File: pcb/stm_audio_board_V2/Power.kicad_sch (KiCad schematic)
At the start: 27 parts, among them U2 OP275, U4 OP275, U5 AMS1117-3.3, U8 L78M09CDT, U9 LF33_TO252

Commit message: Update .mxproject, subdir.mk, and 1078 more files...
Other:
- note added: "18V to 5V COMMON TODO"
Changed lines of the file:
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@@
+    (fill (type none))
+  )
+  (rectangle (start 16.51 74.93) (end 120.65 121.92)
+    (stroke (width 0) (type default))
     (fill (type none))
   )
@@
     (effects (font (size 1.27 1.27)) (justify left bottom))
   )
+  (text "18V to 5V COMMON TODO\n" (at 16.51 73.66 0)
+    (effects (font (size 1.27 1.27)) (justify left bottom))
+  )

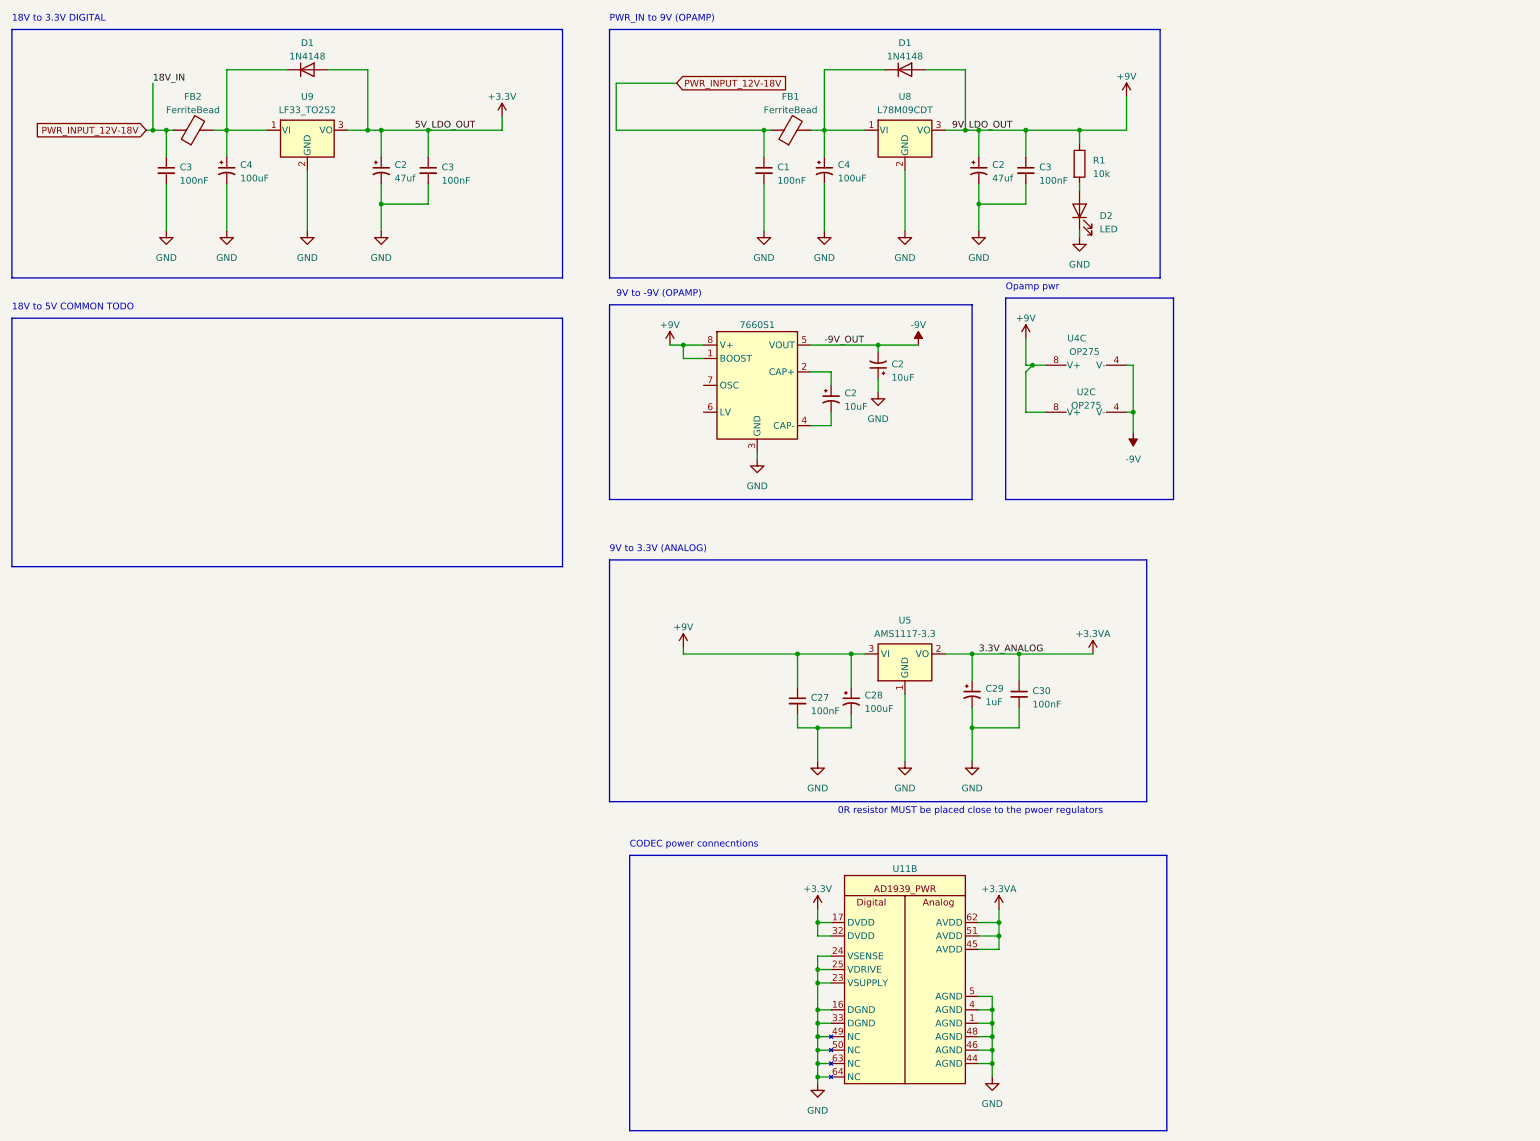
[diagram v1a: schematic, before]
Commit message: pinout added, pcb is updated according to pinout excel
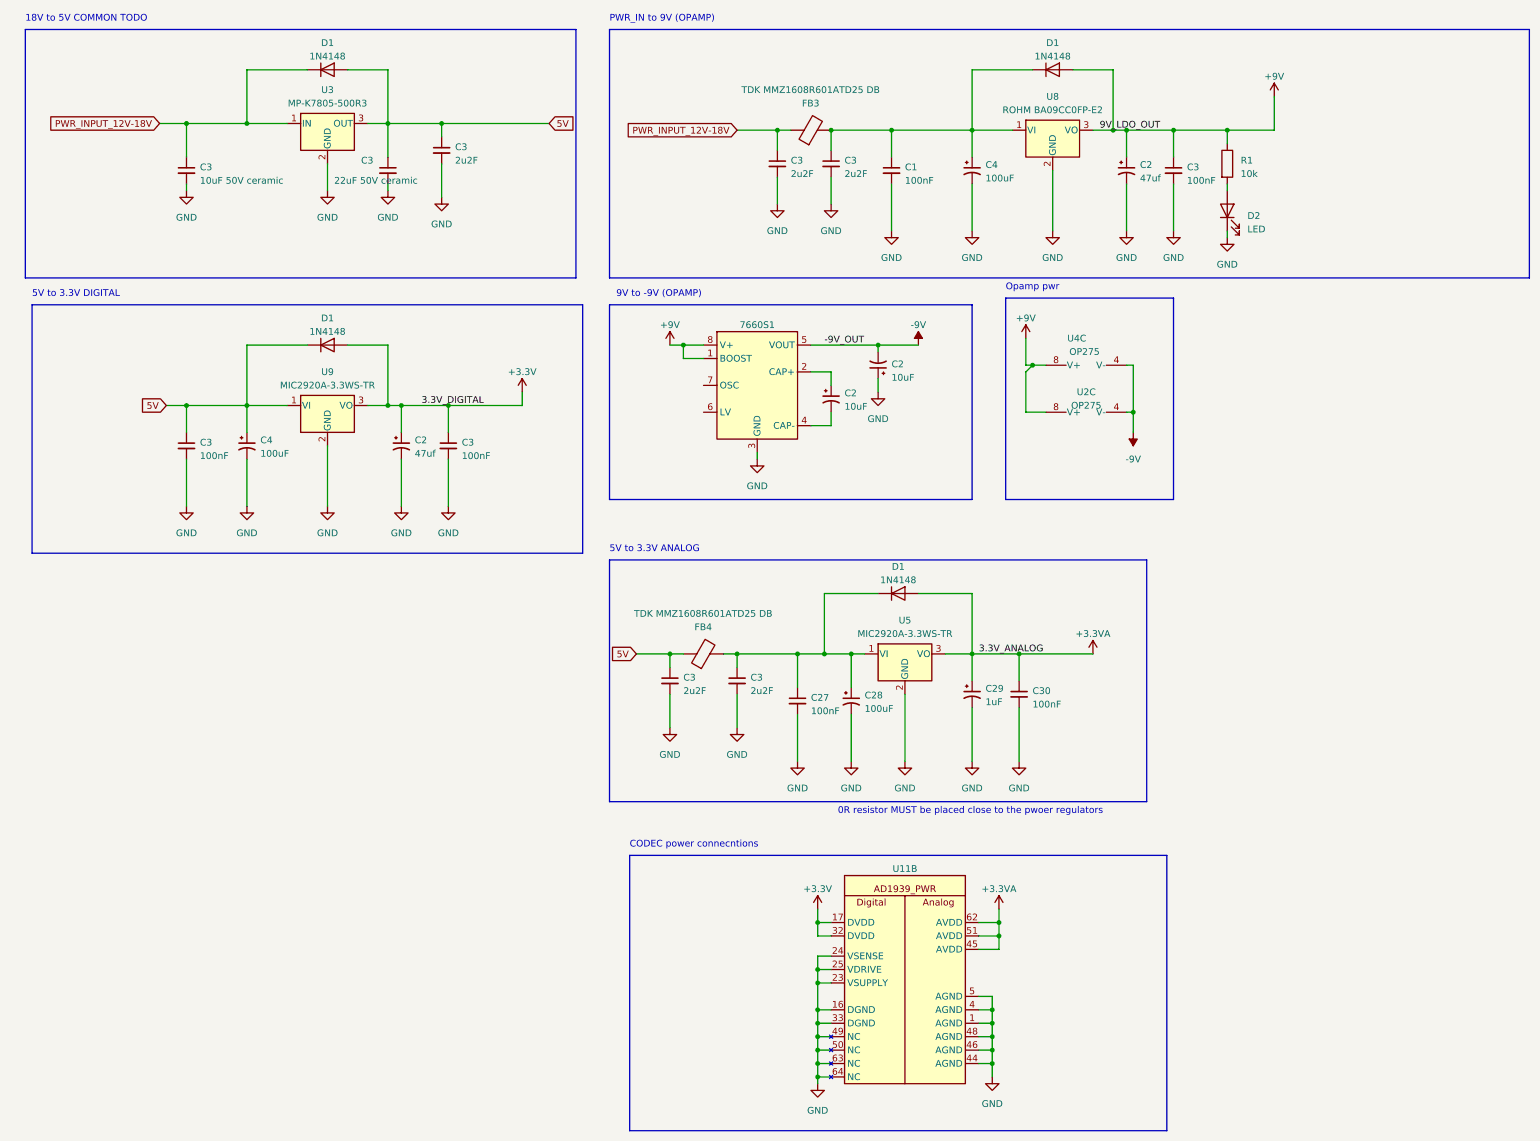
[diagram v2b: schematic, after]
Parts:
- removed FB1, FB2: FerriteBead, Resistor_SMD:R_0603_1608Metric_Pad0.98x0.95mm_HandSolder, symbol Device:FerriteBead
- removed U5: AMS1117-3.3, Package_TO_SOT_SMD:SOT-223-3_TabPin2, symbol Regulator_Linear:AMS1117-3.3
- added C3 (x5): 2u2F, Capacitor_SMD:C_0603_1608Metric_Pad1.08x0.95mm_HandSolder, symbol Device:C_Small
- added C3: 22uF 50V ceramic, Capacitor_SMD:C_0603_1608Metric_Pad1.08x0.95mm_HandSolder, symbol Device:C_Small
- added C3: 10uF 50V ceramic, Capacitor_SMD:C_0603_1608Metric_Pad1.08x0.95mm_HandSolder, symbol Device:C_Small
- added D1 (x2): 1N4148, Diode_THT:D_DO-35_SOD27_P7.62mm_Horizontal, symbol Diode:1N4148
- added FB3, FB4: TDK MMZ1608R601ATD25 DB, Resistor_SMD:R_0603_1608Metric_Pad0.98x0.95mm_HandSolder, symbol Device:FerriteBead
- added U3: MP-K7805-500R3, Package_TO_SOT_THT:TO-220-3_Vertical, symbol Regulator_Linear:L7805
- added U5: MIC2920A-3.3WS-TR, Package_TO_SOT_SMD:SOT-223, symbol Regulator_Linear:LF33_TO252
- U8: value L78M09CDT -> ROHM BA09CC0FP-E2; footprint Package_TO_SOT_SMD:TO-252-2 -> Package_TO_SOT_SMD:TO-252-3_TabPin2
- U9: value LF33_TO252 -> MIC2920A-3.3WS-TR; footprint Package_TO_SOT_SMD:TO-252-2 -> Package_TO_SOT_SMD:SOT-223
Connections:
- net +3.3VA: now also D1.2 (A), U5.3 (VO)
- net +9V: no longer C27.1, C28.1
- net GND: now also C3.2, C3.2, C3.2, C3.2, C3.2, C3.2, C3.2, U3.2 (GND), U5.2 (GND)
- net PWR_INPUT_12V-18V: now also C3.1, C3.1, D1.1 (K), FB3.1, U3.1 (IN); no longer C1.1, C3.1
- net at C4.1, D1.1 (K), U8.1 (VI): now also C1.1, C3.1, FB3.2
- net 5V: now reaches C4.1, D1.1 (K), U9.1 (VI)
- net 5V: now also C3.1, C3.1, C3.1, C3.1, D1.2 (A), FB4.1, U3.3 (OUT)
- new net: C27.1, C28.1, C3.1, D1.1 (K), FB4.2, U5.1 (VI)
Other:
- note added: "5V to 3.3V ANALOG"
- note added: "5V to 3.3V DIGITAL"
- note removed: "18V to 3.3V DIGITAL"
- note removed: "9V to 3.3V (ANALOG)"
- moved on the sheet: C1, C2, C3, C4, D1, D2, R1, U8, U9

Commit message: pinsetup ready
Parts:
- removed C3: 10uF 50V ceramic, Capacitor_SMD:C_0603_1608Metric_Pad1.08x0.95mm_HandSolder, symbol Device:C_Small
- added C4: 22uF 50V ceramic, Capacitor_THT:CP_Radial_D6.3mm_P2.50mm, symbol Device:C_Polarized_Small_US
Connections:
- net GND: now also C4.2
- net PWR_INPUT_12V-18V: now also C4.1
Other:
- moved on the sheet: C3

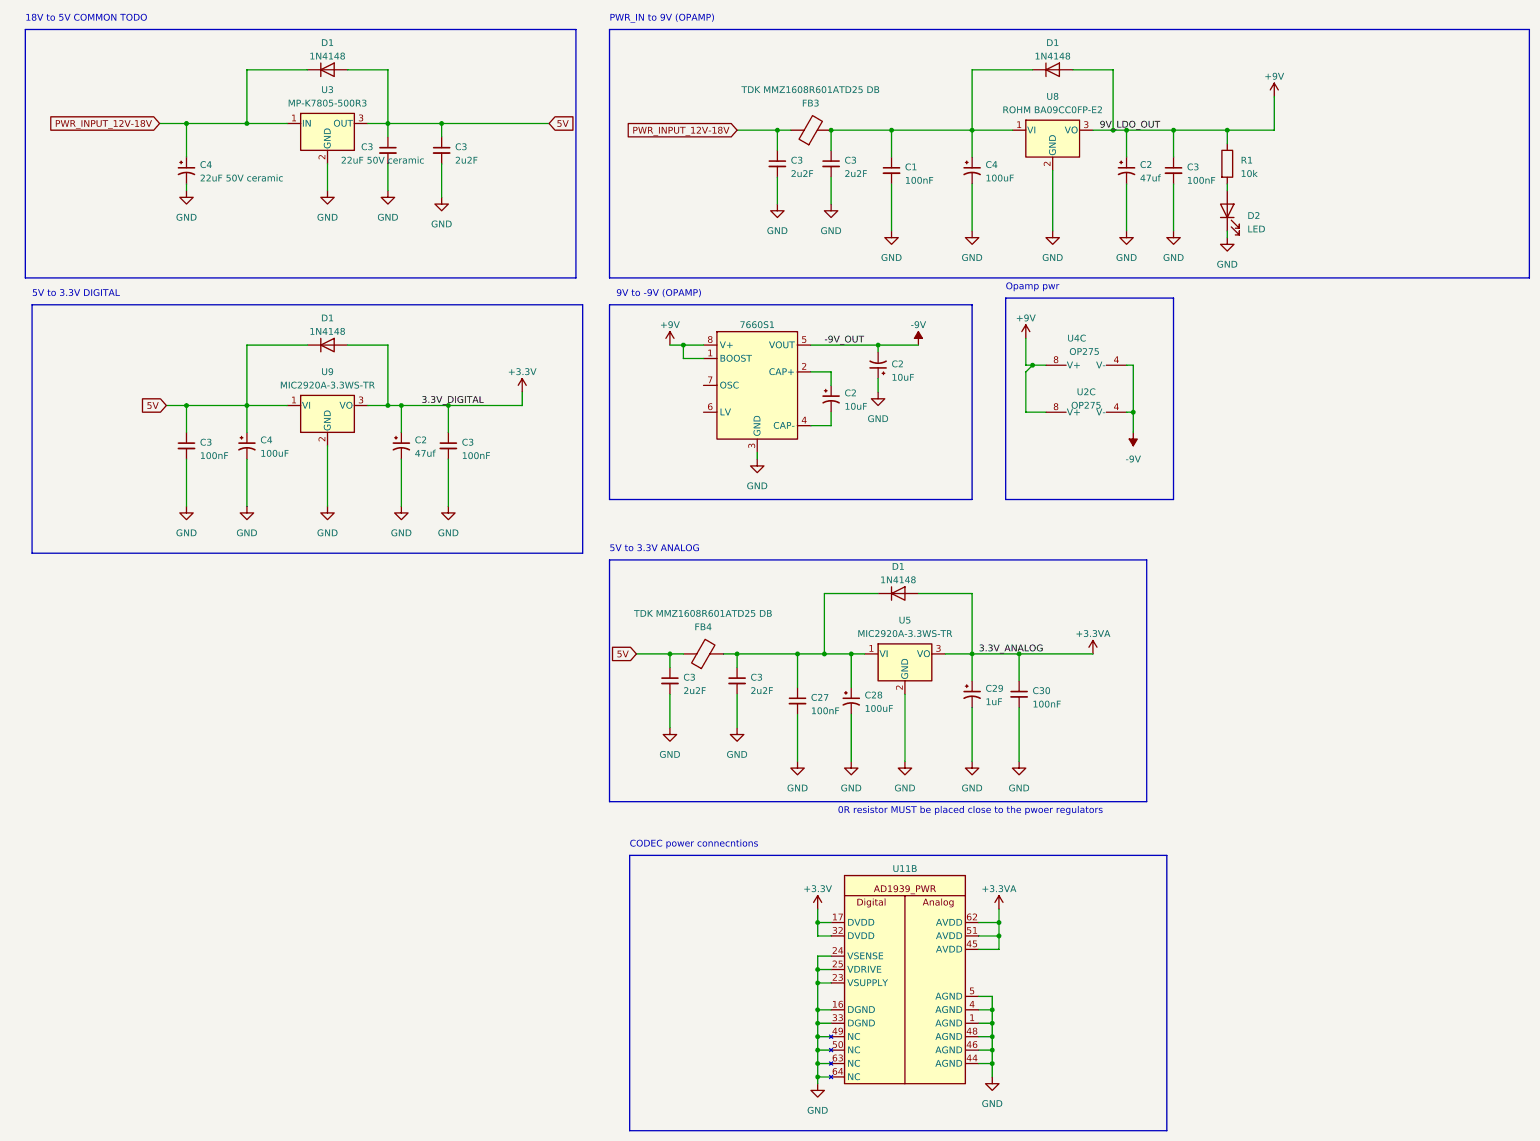
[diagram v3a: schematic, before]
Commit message: Capacitor types are choosen, schematic updated, unused capacitors deleted. Connectors need to be connected to the mcu and its finished
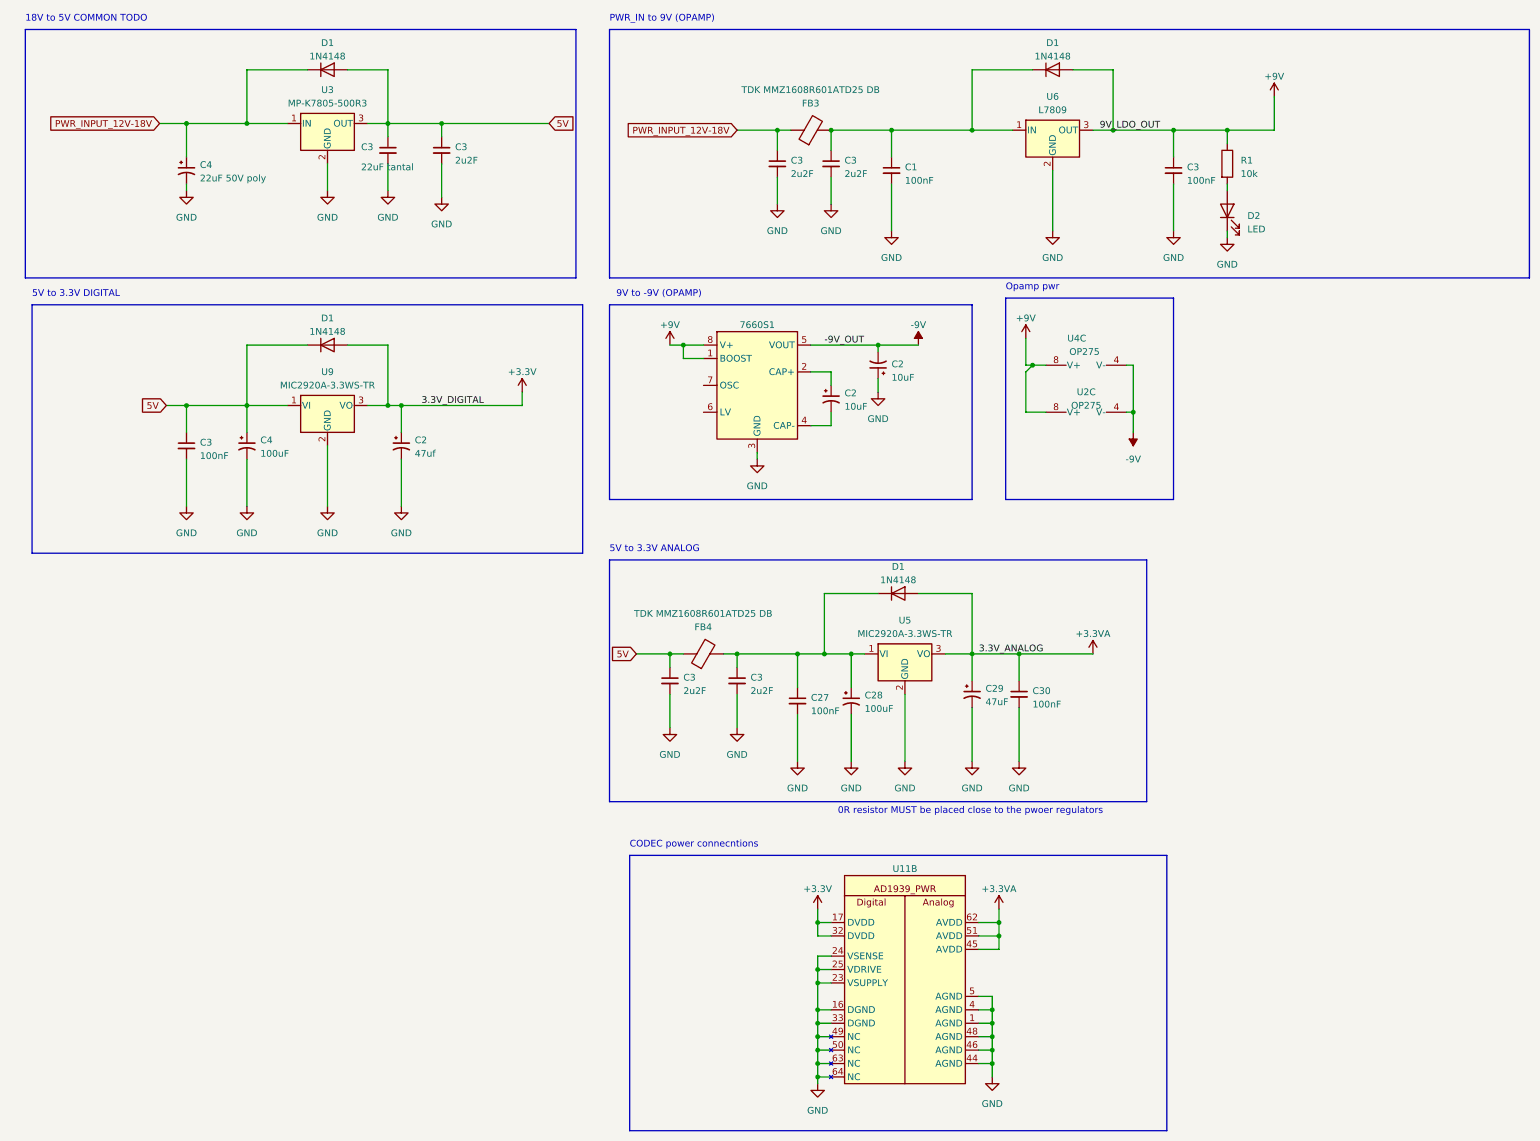
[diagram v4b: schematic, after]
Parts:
- removed C2: 47uf, Capacitor_THT:CP_Radial_D6.3mm_P2.50mm, symbol Device:C_Polarized_Small_US
- removed C3: 100nF, Capacitor_SMD:C_0603_1608Metric_Pad1.08x0.95mm_HandSolder, symbol Device:C_Small
- removed C4: 100uF, Capacitor_SMD:C_1206_3216Metric_Pad1.33x1.80mm_HandSolder, symbol Device:C_Polarized_Small_US
- removed U8: ROHM BA09CC0FP-E2, Package_TO_SOT_SMD:TO-252-3_TabPin2, symbol Regulator_Linear:LF90_TO252
- added U6: L7809, Package_TO_SOT_THT:TO-92_Inline, symbol Regulator_Linear:L7809
- C2: footprint Capacitor_Tantalum_SMD:CP_EIA-7343-31_Kemet-D_Pad2.25x2.55mm_HandSolder -> Capacitor_THT:CP_Radial_D5.0mm_P2.00mm
- C28: footprint Capacitor_Tantalum_SMD:CP_EIA-7343-31_Kemet-D_Pad2.25x2.55mm_HandSolder -> Capacitor_THT:CP_Radial_D6.3mm_P2.50mm
- C29: value 1uF -> 47uF; footprint Capacitor_Tantalum_SMD:CP_EIA-7343-31_Kemet-D_Pad2.25x2.55mm_HandSolder -> Capacitor_THT:CP_Radial_D6.3mm_P2.50mm
- C3: footprint Capacitor_SMD:C_0603_1608Metric_Pad1.08x0.95mm_HandSolder -> Capacitor_SMD:C_0805_2012Metric_Pad1.18x1.45mm_HandSolder
- C3: value 22uF 50V ceramic -> 22uF tantal; footprint Capacitor_SMD:C_0603_1608Metric_Pad1.08x0.95mm_HandSolder -> Capacitor_Tantalum_SMD:CP_EIA-7343-31_Kemet-D_Pad2.25x2.55mm_HandSolder
- C4: value 22uF 50V ceramic -> 22uF 50V poly; footprint Capacitor_THT:CP_Radial_D6.3mm_P2.50mm -> Capacitor_THT:CP_Radial_D5.0mm_P2.00mm
- D1: footprint Diode_THT:D_DO-35_SOD27_P7.62mm_Horizontal -> Diode_SMD:D_1206_3216Metric_Pad1.42x1.75mm_HandSolder
- U5, U9: footprint Package_TO_SOT_SMD:SOT-223 -> Package_TO_SOT_SMD:SOT-223-3_TabPin2
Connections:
- net +9V: now also U6.3 (OUT)
- net GND: now also U6.2 (GND)
- net at C1.1, C3.1, D1.1 (K)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: now also U6.1 (IN)
